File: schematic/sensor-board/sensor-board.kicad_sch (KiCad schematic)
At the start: 6 parts, among them J1 Conn_01x04_Pin, J2 Conn_01x10_Socket, J3 Screw_Terminal_01x03, J4 Screw_Terminal_01x03

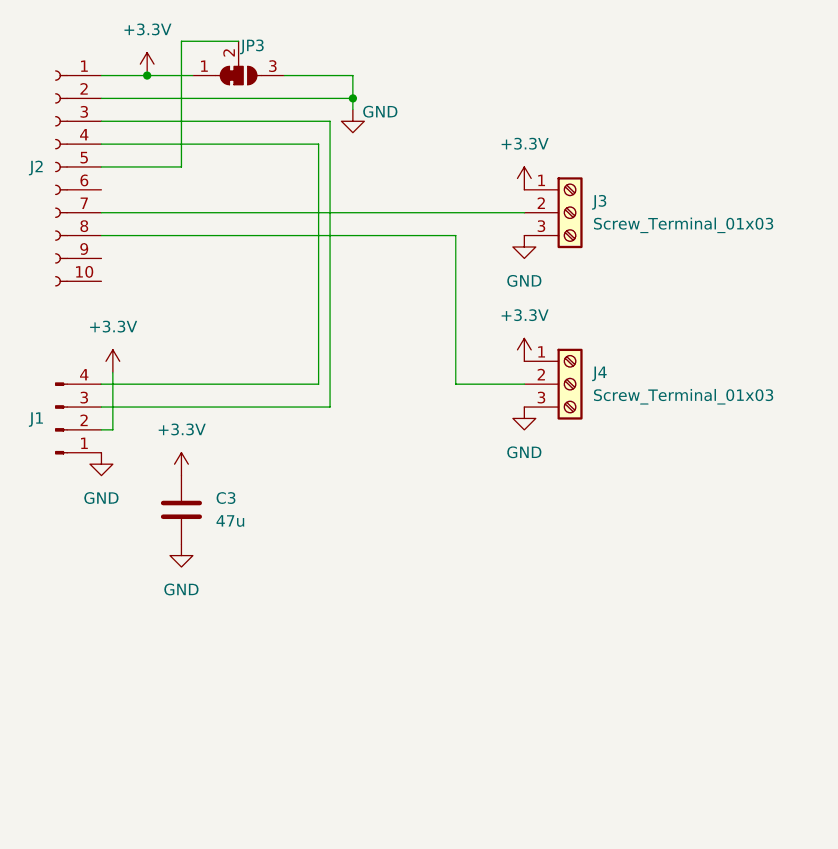
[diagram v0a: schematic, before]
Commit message: updated net labels for pcb layout, added sender board
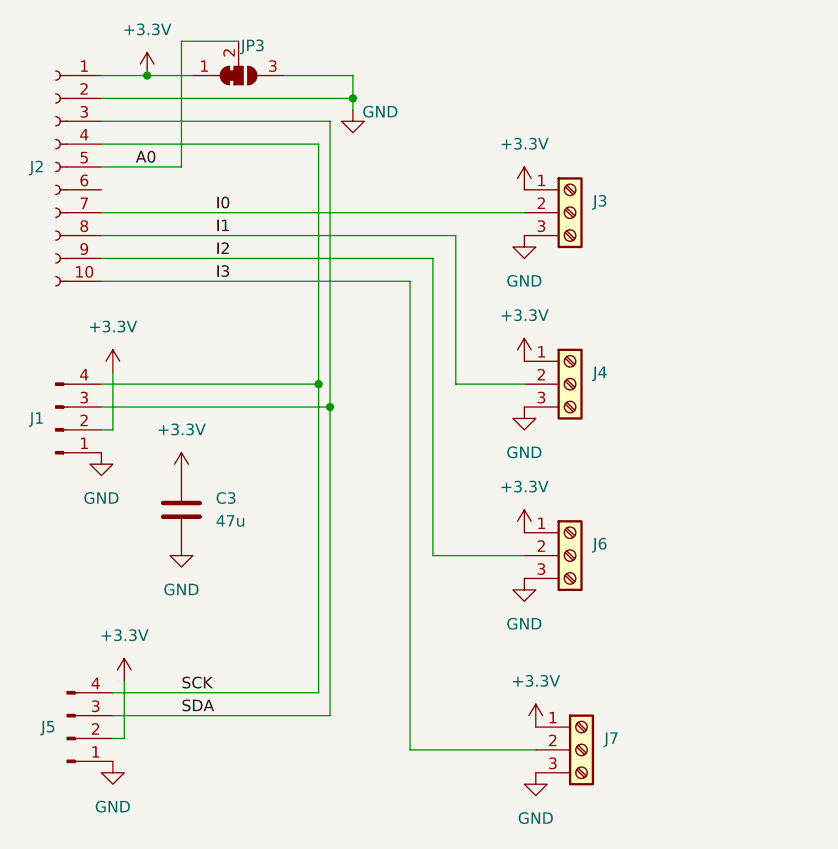
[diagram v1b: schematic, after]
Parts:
- added J5: Conn_01x04_Pin, Connector_PinHeader_2.54mm:PinHeader_1x04_P2.54mm_Vertical, symbol Connector:Conn_01x04_Pin
- added J6, J7: Screw_Terminal_01x03, TerminalBlock_Phoenix:TerminalBlock_Phoenix_MKDS-1,5-3-5.08_1x03_P5.08mm_Horizontal, symbol Connector:Screw_Terminal_01x03
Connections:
- net +3.3V: now also J5.2 (Pin_2), J6.1 (Pin_1), J7.1 (Pin_1)
- net GND: now also J5.1 (Pin_1), J6.3 (Pin_3), J7.3 (Pin_3)
- net I3: now reaches J2.10 (Pin_10)
- net I3: now also J7.2 (Pin_2)
- net SDA: now reaches J1.3 (Pin_3), J2.3 (Pin_3)
- net SDA: now also J5.3 (Pin_3)
- net SCK: now reaches J1.4 (Pin_4), J2.4 (Pin_4)
- net SCK: now also J5.4 (Pin_4)
- net A0: now reaches J2.5 (Pin_5), JP3.2 (C)
- net I0: now reaches J2.7 (Pin_7), J3.2 (Pin_2)
- net I1: now reaches J2.8 (Pin_8), J4.2 (Pin_2)
- net I2: now reaches J2.9 (Pin_9)
- net I2: now also J6.2 (Pin_2)
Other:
- title: (none) -> Makeomatic Sensor Board (ASD1115)
